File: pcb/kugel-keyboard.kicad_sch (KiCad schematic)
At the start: 34 parts, among them SW1 MX_SW_HS, SW10 MX_SW_HS, SW11 MX_SW_HS, SW12 MX_SW_HS, SW13 MX_SW_HS, SW14 MX_SW_HS, SW15 MX_SW_HS, SW16 MX_SW_HS, SW17 MX_SW_HS, SW2 MX_SW_HS, SW3 MX_SW_HS, SW4 MX_SW_HS, SW5 MX_SW_HS, SW6 MX_SW_HS, SW7 MX_SW_HS, SW8 MX_SW_HS, SW9 MX_SW_HS

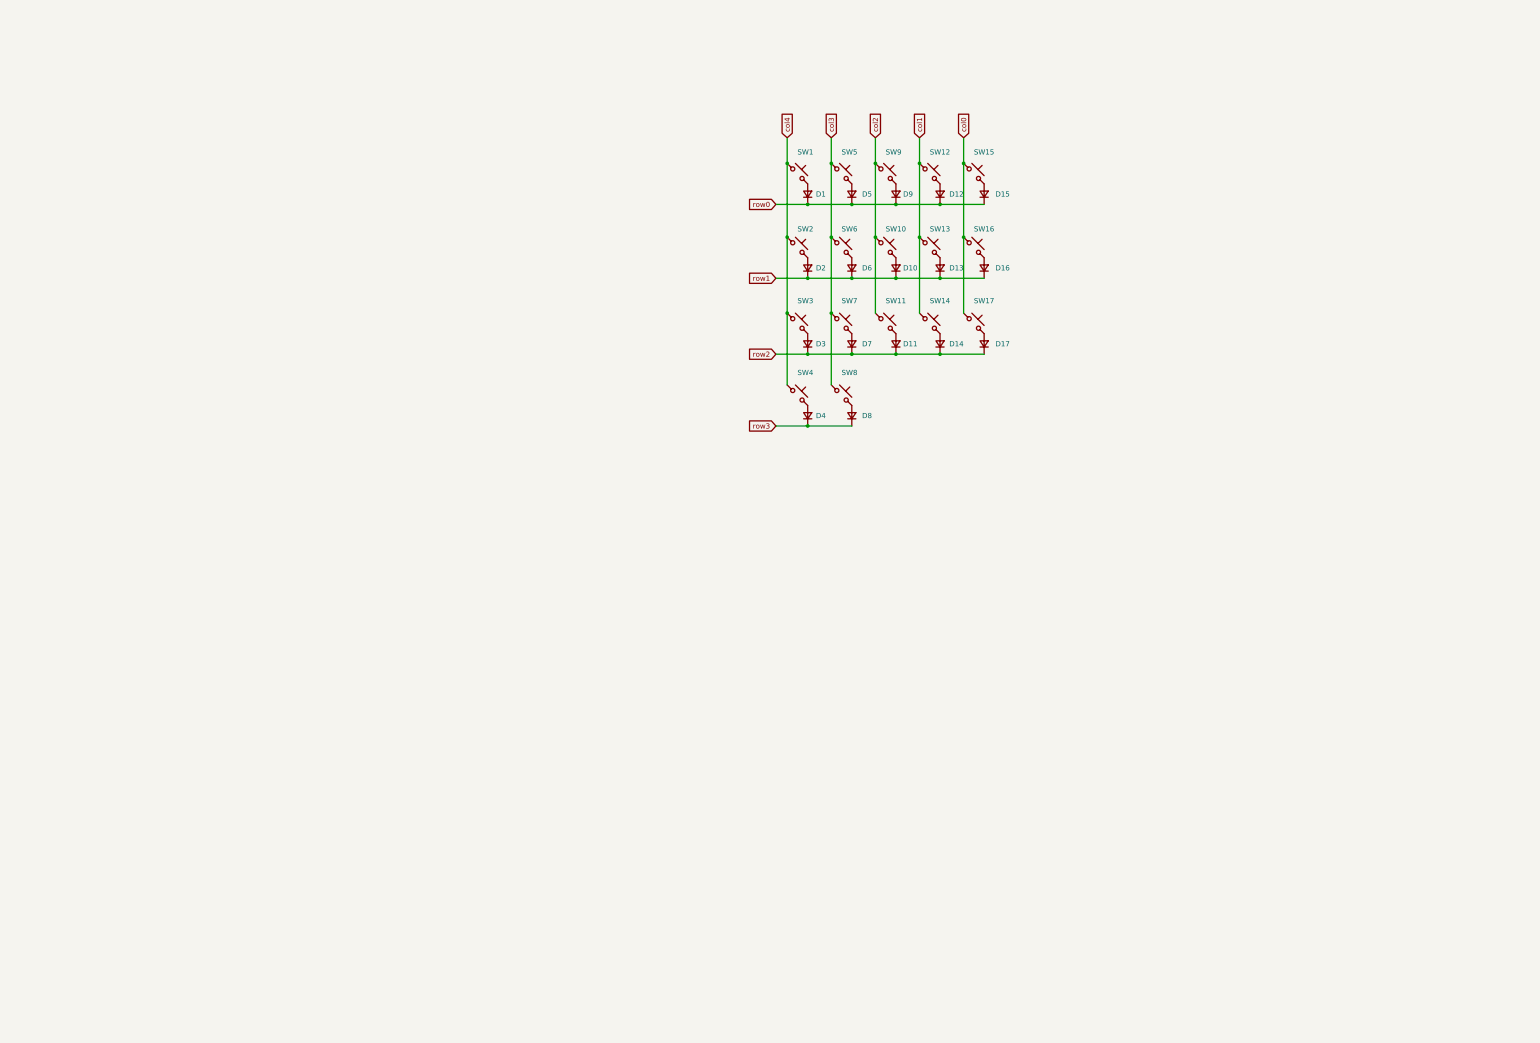
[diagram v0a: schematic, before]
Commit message: added right side PCB and GPIO breakout PCB
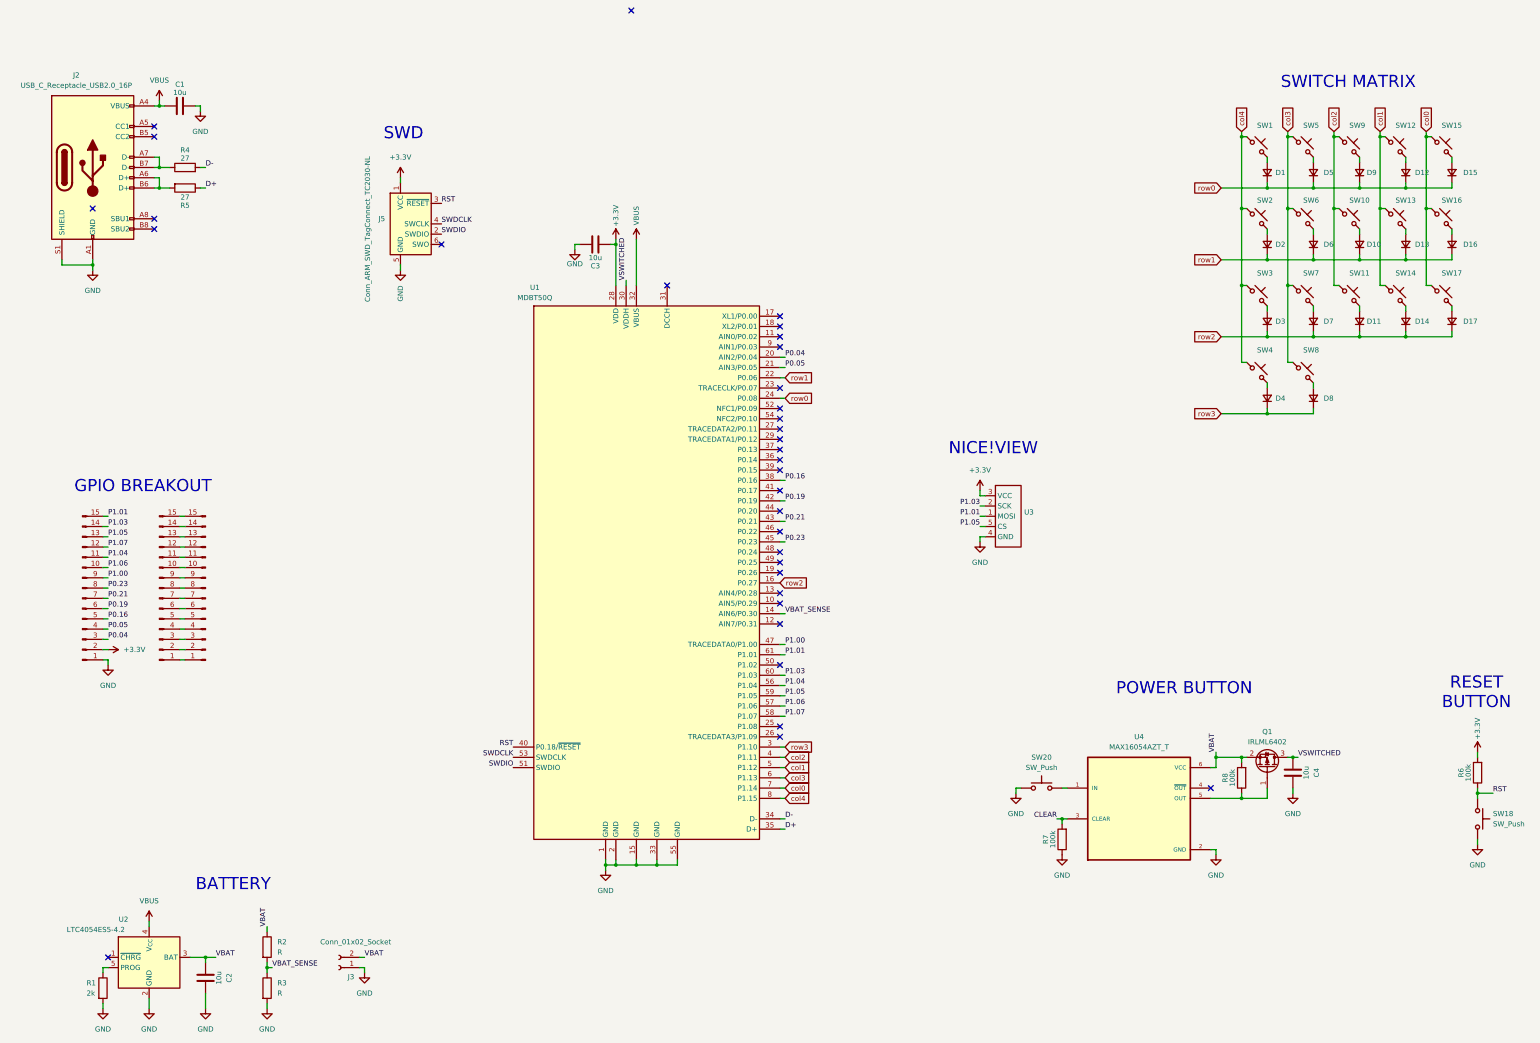
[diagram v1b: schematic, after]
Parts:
- added C1, C2, C3, C4: 10u, Capacitor_SMD:C_0603_1608Metric_Pad1.08x0.95mm_HandSolder, symbol Device:C
- added J1, J6: Conn_01x15_Pin, Connector_FFC-FPC:Hirose_FH12-15S-0.5SH_1x15-1MP_P0.50mm_Horizontal, symbol Connector:Conn_01x15_Pin
- added J2: USB_C_Receptacle_USB2.0_16P, Connector_USB:USB_C_Receptacle_GCT_USB4105-xx-A_16P_TopMnt_Horizontal, symbol Connector:USB_C_Receptacle_USB2.0_16P
- added J3: Conn_01x02_Socket, custom-libary:Battery_solder_pads, symbol Connector:Conn_01x02_Socket
- added J4: Conn_01x15_Pin, Connector_PinHeader_2.54mm:PinHeader_1x15_P2.54mm_Vertical, symbol Connector:Conn_01x15_Pin
- added J5: Conn_ARM_SWD_TagConnect_TC2030-NL, Connector:Tag-Connect_TC2030-IDC-NL_2x03_P1.27mm_Vertical, symbol Connector:Conn_ARM_SWD_TagConnect_TC2030-NL
- added Q1: IRLML6402, Package_TO_SOT_SMD:SOT-23, symbol Transistor_FET:IRLML6402
- added R1: 2k, Resistor_SMD:R_0603_1608Metric_Pad0.98x0.95mm_HandSolder, symbol Device:R
- added R2, R3: R, Resistor_SMD:R_0603_1608Metric_Pad0.98x0.95mm_HandSolder, symbol Device:R
- added R4, R5: 27, Resistor_SMD:R_0603_1608Metric_Pad0.98x0.95mm_HandSolder, symbol Device:R
- added R6, R7, R8: 100k, Resistor_SMD:R_0603_1608Metric_Pad0.98x0.95mm_HandSolder, symbol Device:R
- added SW18, SW20: SW_Push, custom-libary:SW_TL6340AF160Q, symbol Switch:SW_Push
- added U1: MDBT50Q, custom-libary:MDBT50Q-1MV2, symbol custom-libary:MDBT50Q
- added U2: LTC4054ES5-4.2, Package_TO_SOT_SMD:TSOT-23-5, symbol Battery_Management:LTC4054ES5-4.2
- added U3: ~, custom-libary:nice!view, symbol custom-libary:nice!view
- added U4: MAX16054AZT_T, custom-libary:SOT95P275X110-6N, symbol custom-libary:MAX16054AZT_T
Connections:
- net col0: now also U1.7 (P1.14)
- net col1: now also U1.5 (P1.12)
- net col2: now also U1.4 (P1.11)
- net col3: now also U1.6 (P1.13)
- net col4: now also U1.8 (P1.15)
- net row0: now also U1.24 (P0.08)
- net row1: now also U1.22 (P0.06)
- net row2: now also U1.16 (P0.27)
- net row3: now also U1.3 (P1.10)
- new net: J2.A6 (D+), J2.B6 (D+), R5.2
- new net: J2.A7 (D-), J2.B7 (D-), R4.1
- new net: Q1.1 (G), R8.1, U4.5 (OUT)
- new net: J1.1 (Pin_1), J4.1 (Pin_1)
- new net: J1.10 (Pin_10), J4.10 (Pin_10)
- new net: J1.11 (Pin_11), J4.11 (Pin_11)
- new net: J1.12 (Pin_12), J4.12 (Pin_12)
- new net: J1.13 (Pin_13), J4.13 (Pin_13)
- new net: J1.14 (Pin_14), J4.14 (Pin_14)
- new net: J1.15 (Pin_15), J4.15 (Pin_15)
- new net: J1.2 (Pin_2), J4.2 (Pin_2)
- new net: J1.3 (Pin_3), J4.3 (Pin_3)
- new net: J1.4 (Pin_4), J4.4 (Pin_4)
- new net: J1.5 (Pin_5), J4.5 (Pin_5)
- new net: J1.6 (Pin_6), J4.6 (Pin_6)
- new net: J1.7 (Pin_7), J4.7 (Pin_7)
- new net: J1.8 (Pin_8), J4.8 (Pin_8)
- new net: J1.9 (Pin_9), J4.9 (Pin_9)
- new net: SW20.2, U4.1 (IN)
- new net: R1.1, U2.5 (PROG)
- new net +3.3V: C3.1, J5.1 (VCC), J6.2 (Pin_2), R6.2, U1.28 (VDD), U3.3 (VCC)
- new net CLEAR: R7.2, U4.3 (CLEAR)
- new net D+: R5.1, U1.35 (D+)
- new net D-: R4.2, U1.34 (D-)
- new net GND: C1.2, C2.2, C3.2, C4.2, J2.A1 (GND), J2.A12 (GND), J2.B1 (GND), J2.B12 (GND), J2.S1 (SHIELD), J3.1 (Pin_1), J5.5 (GND), J6.1 (Pin_1), R1.2, R3.2, R7.1, SW18.2, SW20.1, U1.1 (GND), U1.15 (GND), U1.2 (GND), U1.33 (GND), U1.55 (GND), U2.2 (GND), U3.4 (GND), U4.2 (GND)
- new net P0.04: J6.3 (Pin_3), U1.20 (AIN2/P0.04)
- new net P0.05: J6.4 (Pin_4), U1.21 (AIN3/P0.05)
- new net P0.16: J6.5 (Pin_5), U1.38 (P0.16)
- new net P0.19: J6.6 (Pin_6), U1.42 (P0.19)
- new net P0.21: J6.7 (Pin_7), U1.43 (P0.21)
- new net P0.23: J6.8 (Pin_8), U1.45 (P0.23)
- new net P1.00: J6.9 (Pin_9), U1.47 (TRACEDATA0/P1.00)
- new net P1.01: J6.15 (Pin_15), U1.61 (P1.01), U3.1 (MOSI)
- new net P1.03: J6.14 (Pin_14), U1.60 (P1.03), U3.2 (SCK)
- new net P1.04: J6.11 (Pin_11), U1.56 (P1.04)
- new net P1.05: J6.13 (Pin_13), U1.59 (P1.05), U3.5 (CS)
- new net P1.06: J6.10 (Pin_10), U1.57 (P1.06)
- new net P1.07: J6.12 (Pin_12), U1.58 (P1.07)
- new net RST: J5.3 (~{RESET}), R6.1, SW18.1, U1.40 (P0.18/~{RESET})
- new net SWDCLK: J5.4 (SWCLK), U1.53 (SWDCLK)
- new net SWDIO: J5.2 (SWDIO), U1.51 (SWDIO)
- new net VBAT: C2.1, J3.2 (Pin_2), Q1.2 (S), R2.1, R8.2, U2.3 (BAT), U4.6 (VCC)
- new net VBAT_SENSE: R2.2, R3.1, U1.14 (AIN6/P0.30)
- new net VBUS: C1.1, J2.A4 (VBUS), J2.A9 (VBUS), J2.B4 (VBUS), J2.B9 (VBUS), U1.32 (VBUS), U2.4 (V_{CC})
- new net VSWITCHED: C4.1, Q1.3 (D), U1.30 (VDDH)
- no-connect marks 0 -> 34
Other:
- note added: "BATTERY"
- note added: "GPIO BREAKOUT"
- note added: "NICE!VIEW"
- note added: "POWER BUTTON"
- note added: "RESET BUTTON"
- note added: "SWD"
- note added: "SWITCH MATRIX"
- moved on the sheet: D1, D10, D11, D12, D13, D14, D15, D16, D17, D2, D3, D4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

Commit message: added left side PCB and GPIO breakout PCB
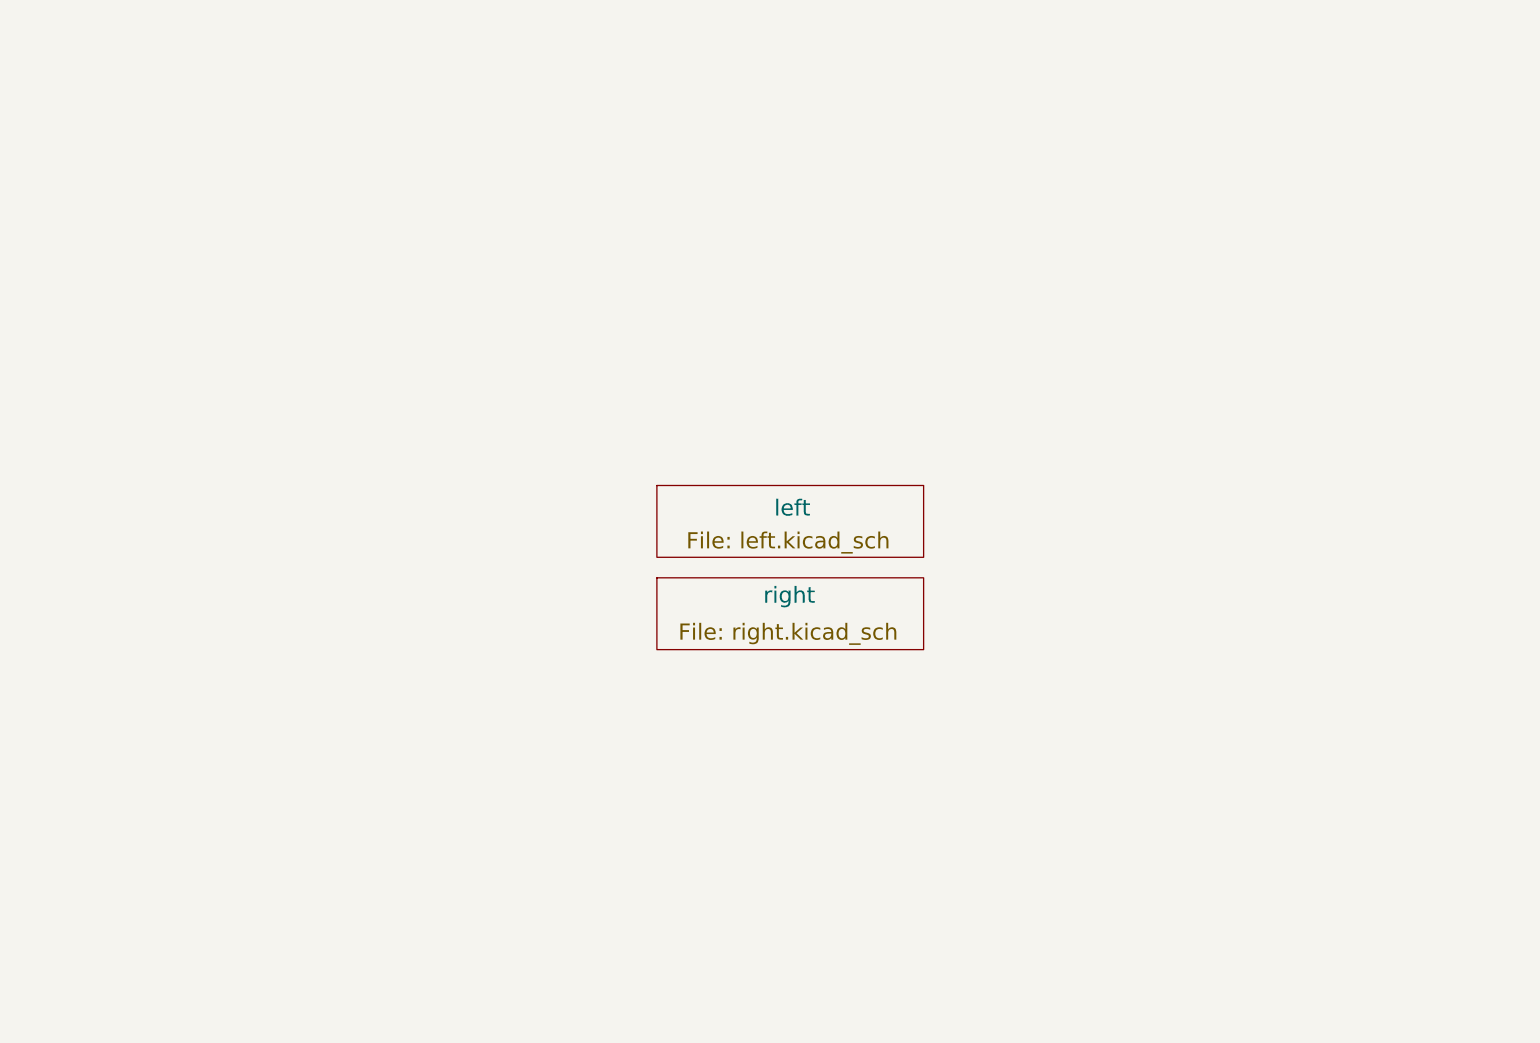
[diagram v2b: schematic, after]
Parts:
- removed C1, C2, C3, C4: 10u, Capacitor_SMD:C_0603_1608Metric_Pad1.08x0.95mm_HandSolder, symbol Device:C
- removed D1, D10, D11, D12, D13, D14, D15, D16, D17, D2, D3, D4, D5, D6, D7, D8, D9: D_Small, Diode_SMD:Nexperia_CFP3_SOD-123W, symbol Device:D_Small
- removed J1, J6: Conn_01x15_Pin, Connector_FFC-FPC:Hirose_FH12-15S-0.5SH_1x15-1MP_P0.50mm_Horizontal, symbol Connector:Conn_01x15_Pin
- removed J2: USB_C_Receptacle_USB2.0_16P, Connector_USB:USB_C_Receptacle_GCT_USB4105-xx-A_16P_TopMnt_Horizontal, symbol Connector:USB_C_Receptacle_USB2.0_16P
- removed J3: Conn_01x02_Socket, custom-libary:Battery_solder_pads, symbol Connector:Conn_01x02_Socket
- removed J4: Conn_01x15_Pin, Connector_PinHeader_2.54mm:PinHeader_1x15_P2.54mm_Vertical, symbol Connector:Conn_01x15_Pin
- removed J5: Conn_ARM_SWD_TagConnect_TC2030-NL, Connector:Tag-Connect_TC2030-IDC-NL_2x03_P1.27mm_Vertical, symbol Connector:Conn_ARM_SWD_TagConnect_TC2030-NL
- removed Q1: IRLML6402, Package_TO_SOT_SMD:SOT-23, symbol Transistor_FET:IRLML6402
- removed R1: 2k, Resistor_SMD:R_0603_1608Metric_Pad0.98x0.95mm_HandSolder, symbol Device:R
- removed R2, R3: R, Resistor_SMD:R_0603_1608Metric_Pad0.98x0.95mm_HandSolder, symbol Device:R
- removed R4, R5: 27, Resistor_SMD:R_0603_1608Metric_Pad0.98x0.95mm_HandSolder, symbol Device:R
- removed R6, R7, R8: 100k, Resistor_SMD:R_0603_1608Metric_Pad0.98x0.95mm_HandSolder, symbol Device:R
- removed SW1, SW5: MX_SW_HS, custom-libary:Kailh_socket_PG1350, symbol KLOTZ:MX_SW_HS
- removed SW10, SW11, SW12, SW13, SW14, SW15, SW16, SW17, SW2, SW3, SW4, SW6, SW7, SW8, SW9: MX_SW_HS, custom-libary:Kailh_socket_PG1350, symbol marbastlib-mx:MX_SW_HS
- removed SW18, SW20: SW_Push, custom-libary:SW_TL6340AF160Q, symbol Switch:SW_Push
- removed U1: MDBT50Q, custom-libary:MDBT50Q-1MV2, symbol custom-libary:MDBT50Q
- removed U2: LTC4054ES5-4.2, Package_TO_SOT_SMD:TSOT-23-5, symbol Battery_Management:LTC4054ES5-4.2
- removed U3: ~, custom-libary:nice!view, symbol custom-libary:nice!view
- removed U4: MAX16054AZT_T, custom-libary:SOT95P275X110-6N, symbol custom-libary:MAX16054AZT_T
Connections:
- no-connect marks 34 -> 0
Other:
- added sheet left (left.kicad_sch)
- added sheet right (right.kicad_sch)
- note removed: "BATTERY"
- note removed: "GPIO BREAKOUT"
- note removed: "NICE!VIEW"
- note removed: "POWER BUTTON"
- note removed: "RESET BUTTON"
- note removed: "SWD"
- note removed: "SWITCH MATRIX"

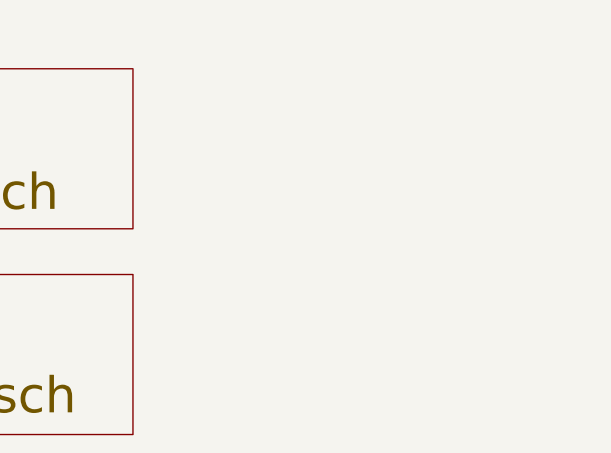
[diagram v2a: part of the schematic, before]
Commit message: added external oszilator
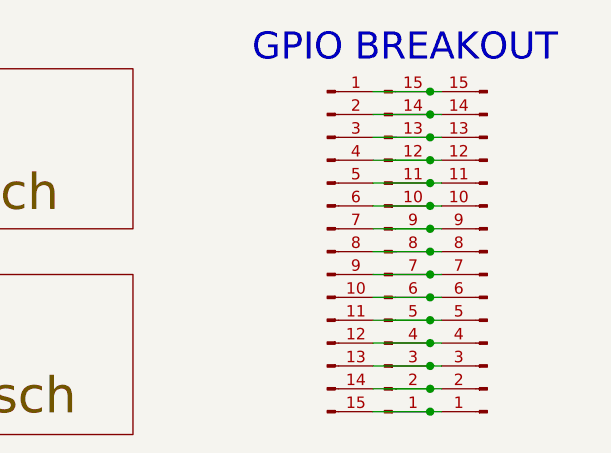
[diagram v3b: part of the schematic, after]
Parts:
- added J1, J13: Conn_01x15_Pin, Connector_FFC-FPC:Hirose_FH12-15S-0.5SH_1x15-1MP_P0.50mm_Horizontal, symbol Connector:Conn_01x15_Pin
- added J4: Conn_01x15_Pin, Connector_PinHeader_2.54mm:PinHeader_1x15_P2.54mm_Vertical, symbol Connector:Conn_01x15_Pin
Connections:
- new net: J1.1 (Pin_1), J13.15 (Pin_15), J4.1 (Pin_1)
- new net: J1.10 (Pin_10), J13.6 (Pin_6), J4.10 (Pin_10)
- new net: J1.11 (Pin_11), J13.5 (Pin_5), J4.11 (Pin_11)
- new net: J1.12 (Pin_12), J13.4 (Pin_4), J4.12 (Pin_12)
- new net: J1.13 (Pin_13), J13.3 (Pin_3), J4.13 (Pin_13)
- new net: J1.14 (Pin_14), J13.2 (Pin_2), J4.14 (Pin_14)
- new net: J1.15 (Pin_15), J13.1 (Pin_1), J4.15 (Pin_15)
- new net: J1.2 (Pin_2), J13.14 (Pin_14), J4.2 (Pin_2)
- new net: J1.3 (Pin_3), J13.13 (Pin_13), J4.3 (Pin_3)
- new net: J1.4 (Pin_4), J13.12 (Pin_12), J4.4 (Pin_4)
- new net: J1.5 (Pin_5), J13.11 (Pin_11), J4.5 (Pin_5)
- new net: J1.6 (Pin_6), J13.10 (Pin_10), J4.6 (Pin_6)
- new net: J1.7 (Pin_7), J13.9 (Pin_9), J4.7 (Pin_7)
- new net: J1.8 (Pin_8), J13.8 (Pin_8), J4.8 (Pin_8)
- new net: J1.9 (Pin_9), J13.7 (Pin_7), J4.9 (Pin_9)
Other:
- note added: "GPIO BREAKOUT"
